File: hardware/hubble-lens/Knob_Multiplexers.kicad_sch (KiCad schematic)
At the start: 25 parts

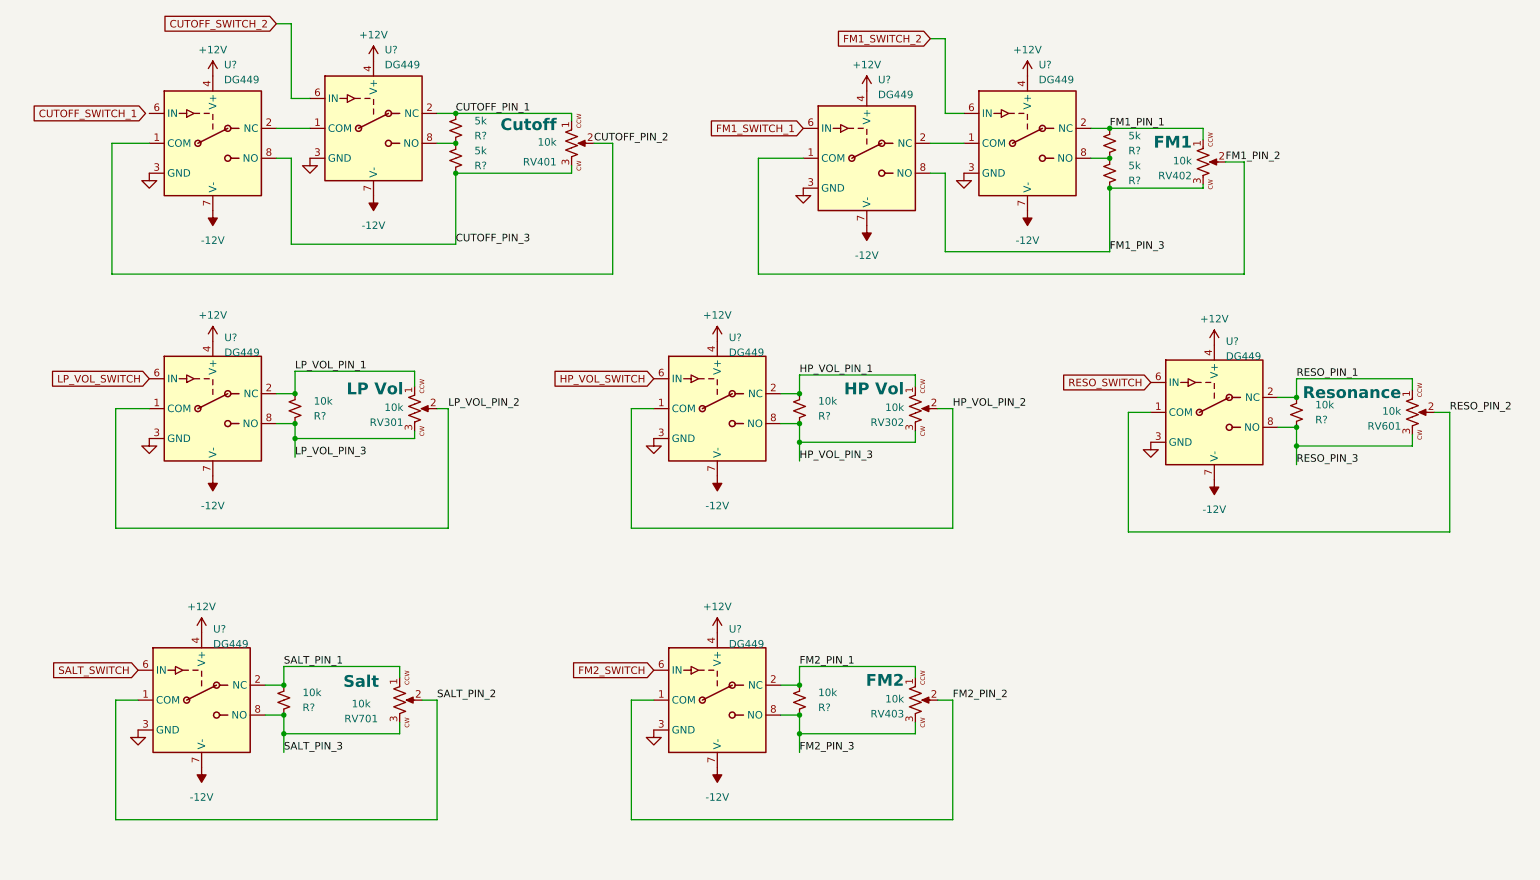
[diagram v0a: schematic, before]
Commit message: Rough Draft of PCB for Hubble Lens
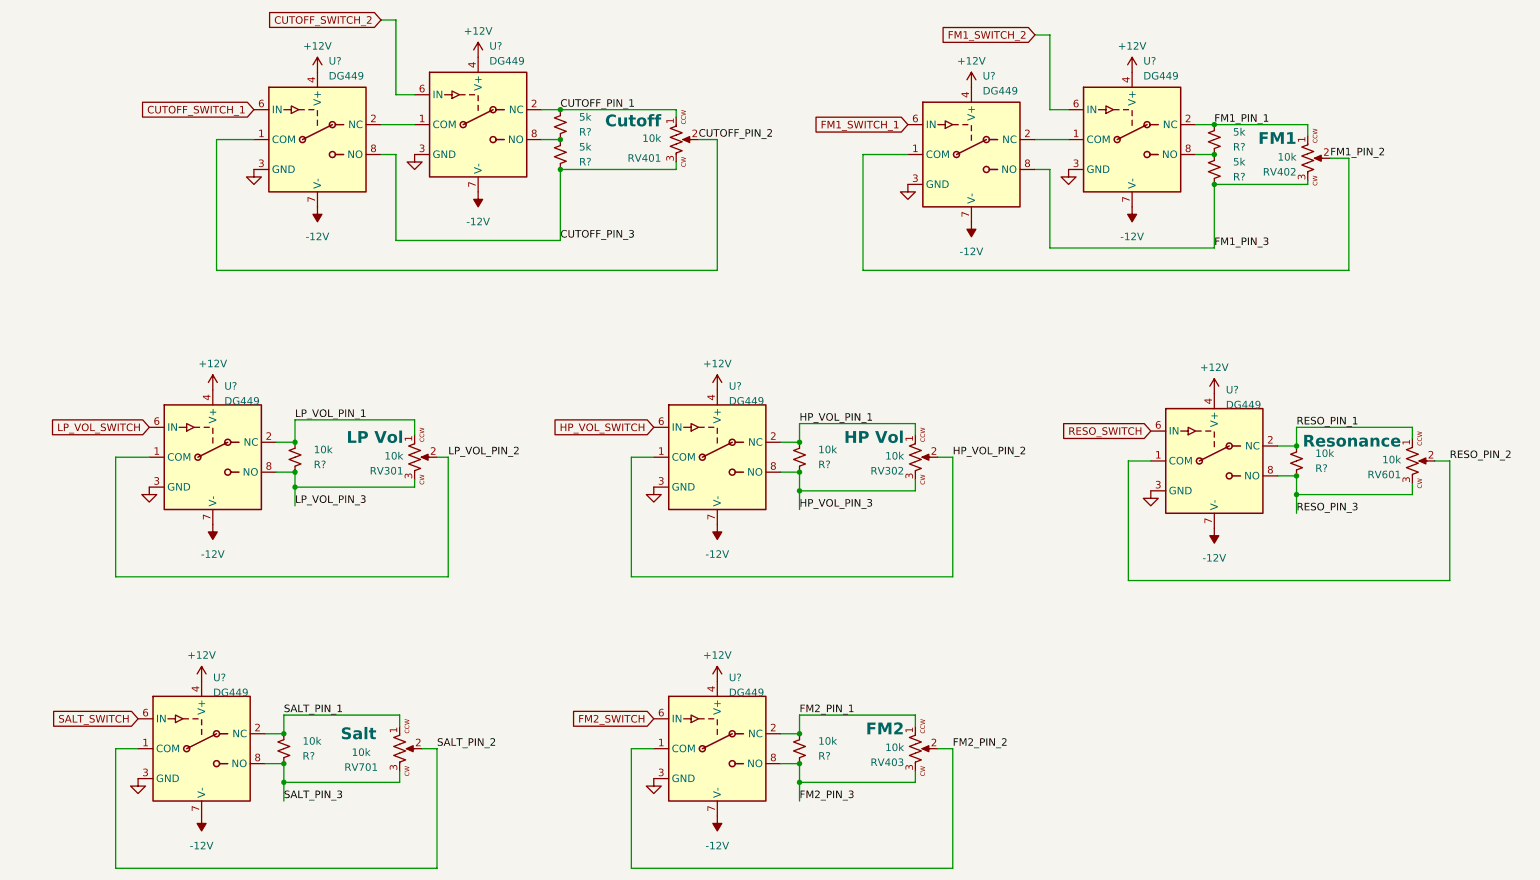
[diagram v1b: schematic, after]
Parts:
- R? (x9): footprint (none) -> winterbloom:R_0603_HandSolder
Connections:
- net CUTOFF_SWITCH_1: now also U?.6 (IN)
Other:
- moved on the sheet: R?, RV301, RV302, RV401, RV402, RV403, RV601, RV701, U?
